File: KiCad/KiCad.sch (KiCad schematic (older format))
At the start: 18 parts

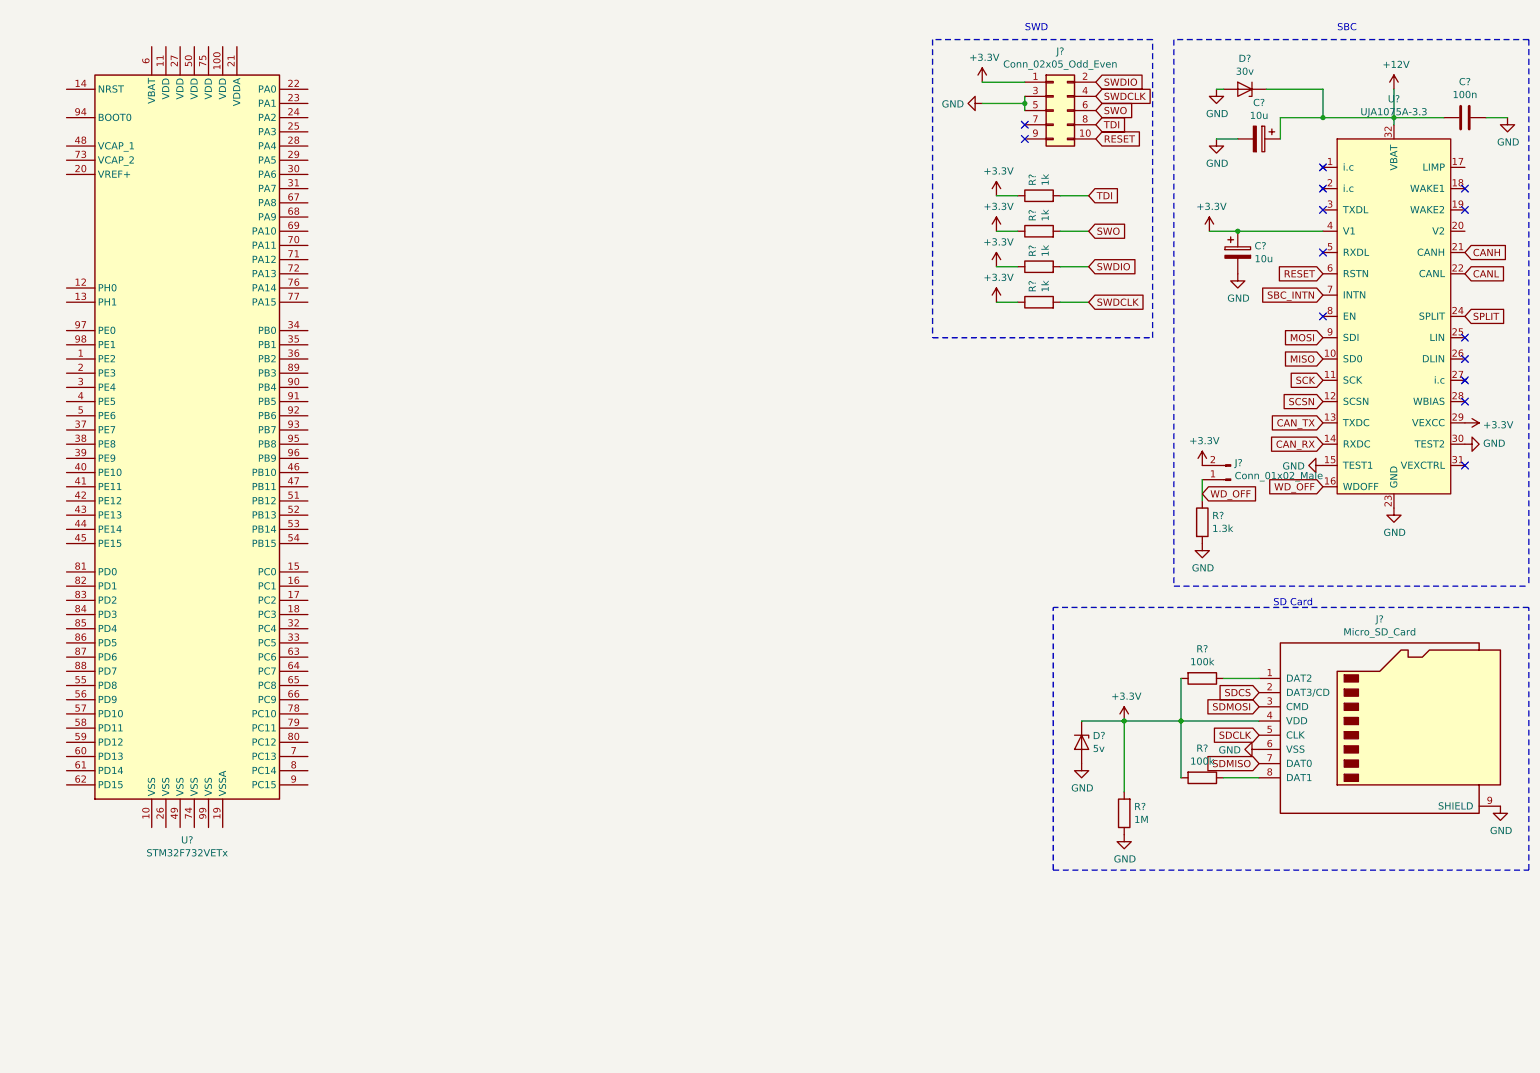
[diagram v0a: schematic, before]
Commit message: SPI, reset, CAN and status
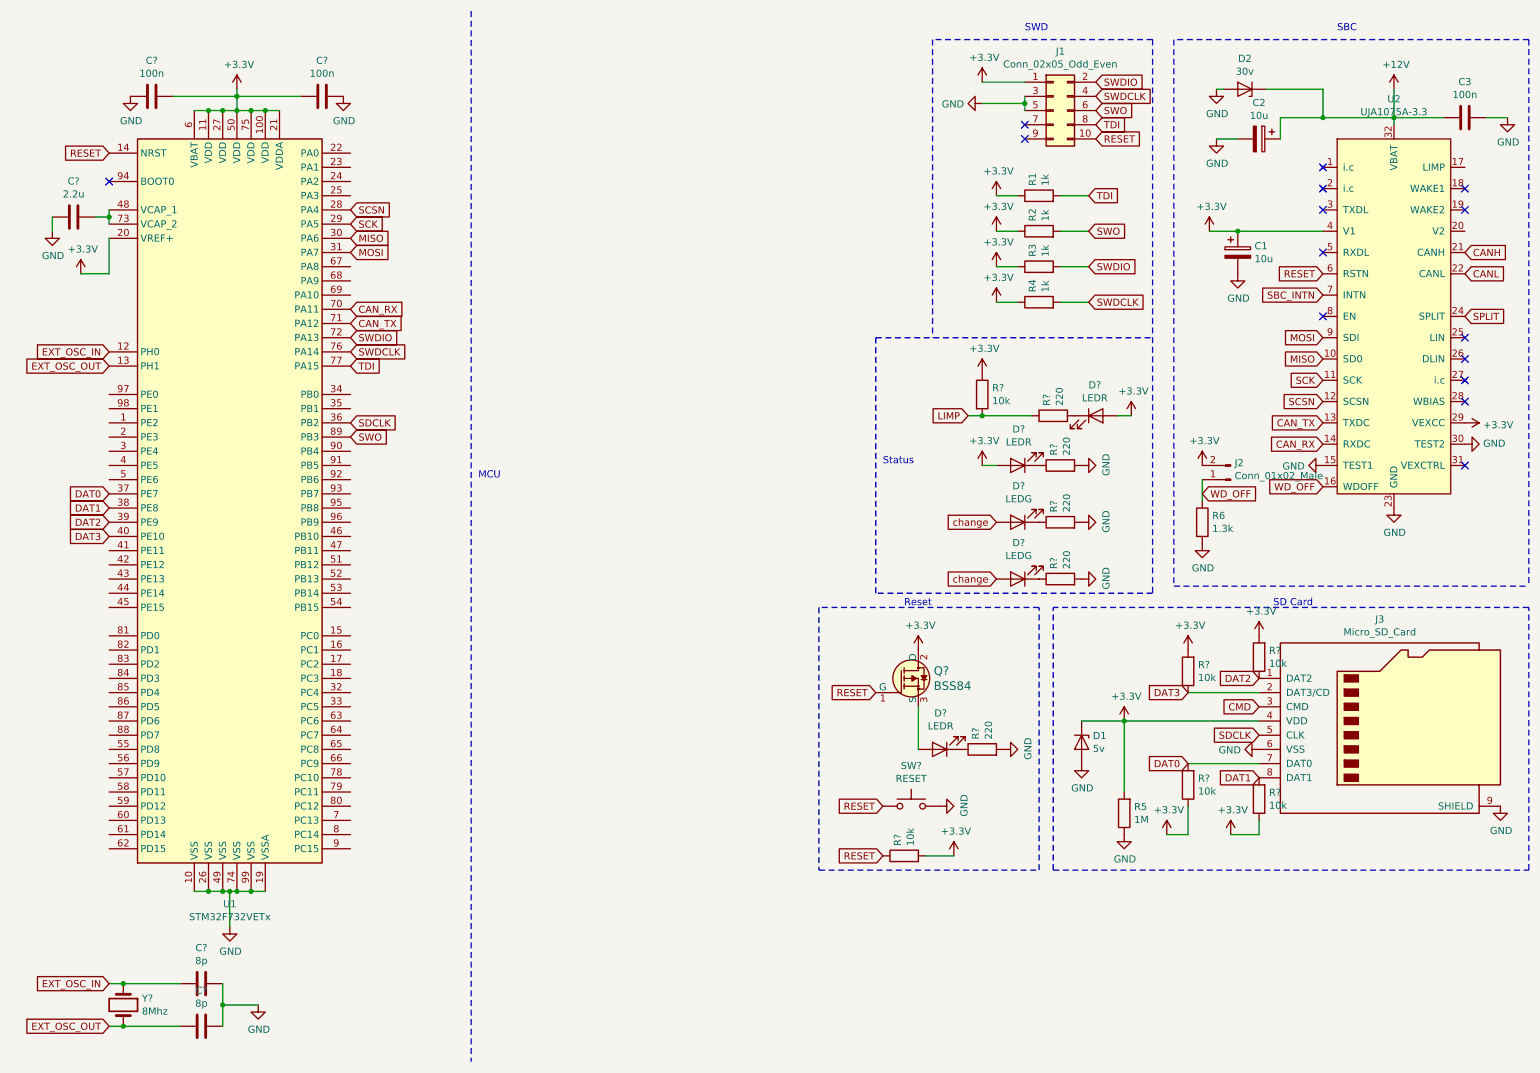
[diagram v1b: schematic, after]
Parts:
- removed R? (x2): 100k, symbol Device:R
- added C? (x2): 100n, Capacitor_SMD:C_0603_1608Metric_Pad1.05x0.95mm_HandSolder, symbol Device:C
- added C?: 2.2u, Capacitor_SMD:C_0603_1608Metric_Pad1.05x0.95mm_HandSolder, symbol Device:C
- added C? (x2): 8p, Capacitor_SMD:C_0603_1608Metric_Pad1.05x0.95mm_HandSolder, symbol Device:C
- added D? (x3): LEDR, symbol Device:LED
- added D? (x2): LEDG, symbol Device:LED
- added Q?: BSS84, digikey-footprints:SOT-23-3, symbol dk_Transistors-FETs-MOSFETs-Single:BSS84
- added R? (x5): 220, Resistor_SMD:R_0603_1608Metric_Pad1.05x0.95mm_HandSolder, symbol Device:R
- added R? (x6): 10k, Resistor_SMD:R_0603_1608Metric_Pad1.05x0.95mm_HandSolder, symbol Device:R
- added SW?: RESET, symbol Switch:SW_Push
- added Y?: 8Mhz, symbol Device:Crystal
- C1, C2, C3: renamed from C?; footprint (none) -> Capacitor_SMD:C_0603_1608Metric_Pad1.05x0.95mm_HandSolder
- R1, R2, R3, R4, R5, R6: renamed from R?; footprint (none) -> Resistor_SMD:R_0603_1608Metric_Pad1.05x0.95mm_HandSolder
- gave numbers to parts that had none: 7
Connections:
- net SDCS is gone; now on net DAT3: J3.2 (DAT3/CD)
- net SDMISO is gone; now on net DAT0: J3.7 (DAT0)
- net +3V3: now also U1.100 (VDD), U1.11 (VDD), U1.20 (VREF+), U1.21 (VDDA), U1.27 (VDD), U1.50 (VDD), U1.6 (VBAT), U1.75 (VDD), C?.1, C?.2, D?.2 (A), D?.2 (A), Q?.2 (D), R?.1, R?.1, R?.1, R?.2, R?.2, R?.2
- net CAN_RX: now also U1.70 (PA11)
- net CAN_TX: now also U1.71 (PA12)
- net GND: now also U1.10 (VSS), U1.19 (VSSA), U1.26 (VSS), U1.49 (VSS), U1.74 (VSS), U1.99 (VSS), C?.1, C?.1, C?.1, C?.2, C?.2, R?.2, R?.2, R?.2, R?.2, SW?.2
- net MISO: now also U1.30 (PA6)
- net MOSI: now also U1.31 (PA7)
- net RESET: now also U1.14 (NRST), Q?.1 (G), R?.1, SW?.1
- net SCK: now also U1.29 (PA5)
- net SCSN: now also U1.28 (PA4)
- net SDCLK: now also U1.36 (PB2)
- net SWDCLK: now also U1.76 (PA14)
- net SWDIO: now also U1.72 (PA13)
- net SWO: now also U1.89 (PB3)
- net TDI: now also U1.77 (PA15)
- net EXT_OSC_IN: now reaches U1.12 (PH0)
- net EXT_OSC_IN: now also C?.2, Y?.1
- net EXT_OSC_OUT: now reaches U1.13 (PH1)
- net EXT_OSC_OUT: now also C?.2, Y?.2
- net DAT0: now reaches U1.37 (PE7)
- net DAT0: now also R?.2
- net DAT1: now reaches U1.38 (PE8)
- net DAT1: now also J3.8 (DAT1), R?.2
- net DAT2: now reaches U1.39 (PE9)
- net DAT2: now also J3.1 (DAT2), R?.1
- net DAT3: now reaches U1.40 (PE10)
- net DAT3: now also R?.1
- net at U1.48 (VCAP_1): now also U1.73 (VCAP_2), C?.1
- net SDMOSI renamed CMD
- new net: D?.2 (A), Q?.3 (S)
- new net: D?.1 (K), R?.1 (x4)
- new net: D?.1 (K), R?.2
- new net LIMP: R?.1, R?.2
- new net change: D?.2 (A), D?.2 (A)
- no-connect marks 14 -> 15
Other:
- note added: "MCU"
- note added: "Reset"
- note added: "Status"
- moved on the sheet: U1

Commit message: Two SBCs and Autogenerated STM32cube code
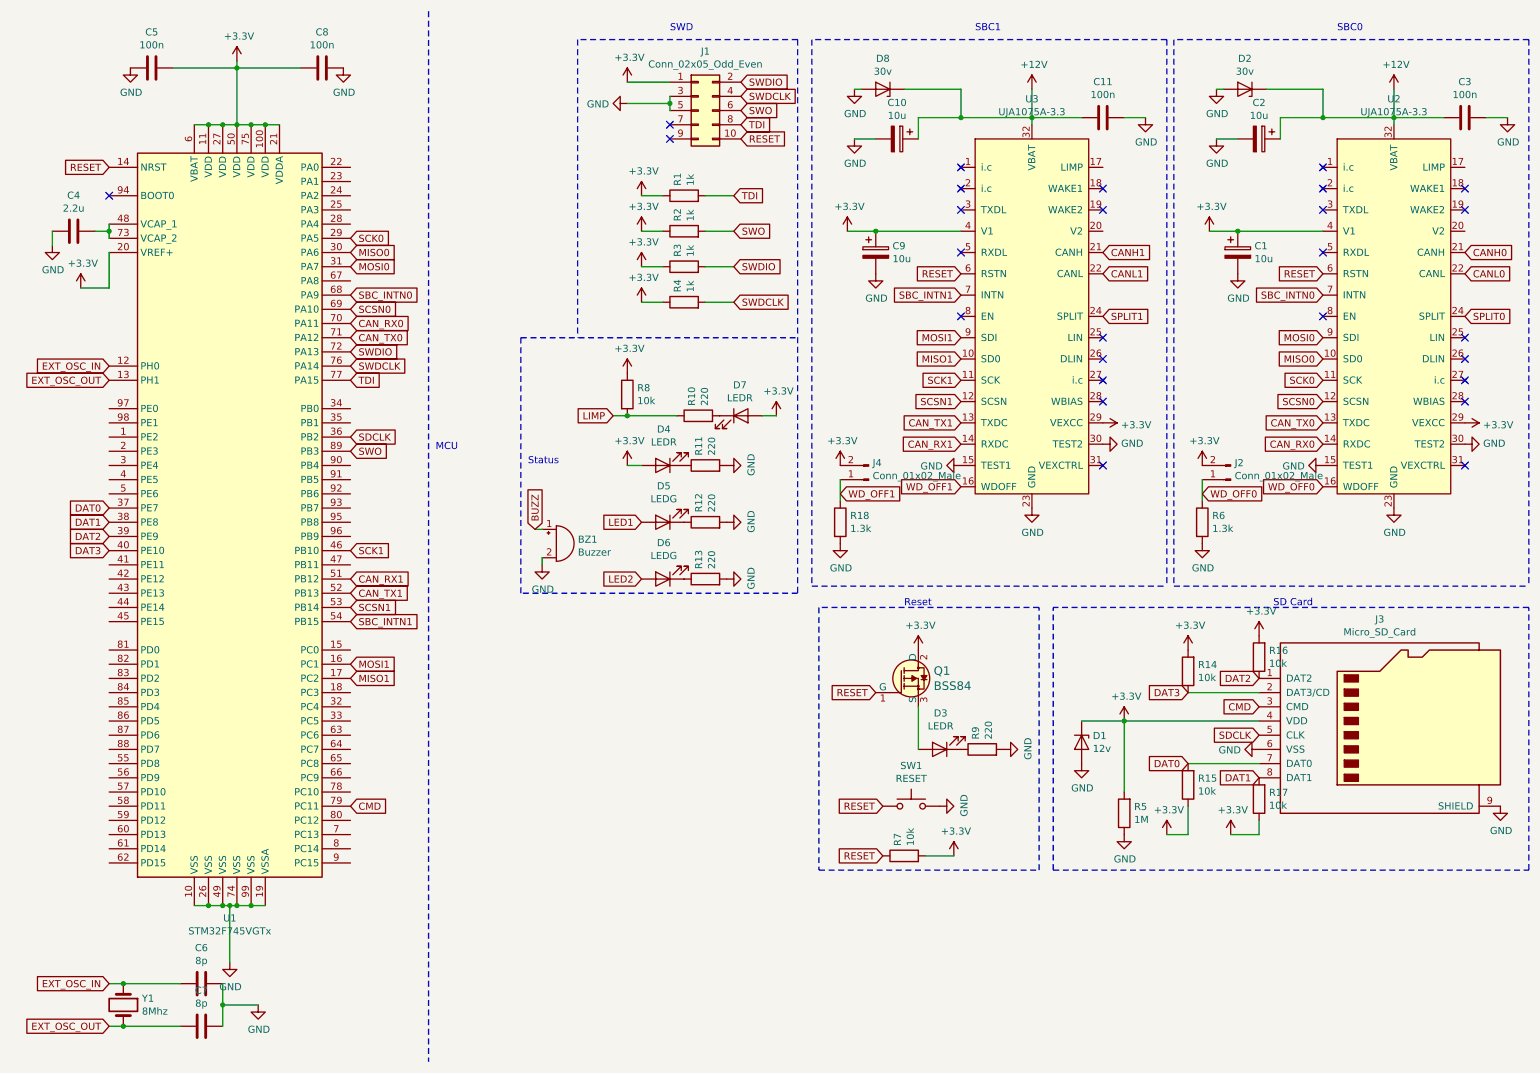
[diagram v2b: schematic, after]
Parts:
- removed U1: STM32F732VETx, Package_QFP:LQFP-100_14x14mm_P0.5mm, symbol MCU_ST_STM32F7:STM32F732VETx
- added BZ1: Buzzer, Buzzer_Beeper:Buzzer_12x9.5RM7.6, symbol Device:Buzzer
- added C10, C9: 10u, Capacitor_SMD:C_0603_1608Metric_Pad1.05x0.95mm_HandSolder, symbol Device:CP
- added C11: 100n, Capacitor_SMD:C_0603_1608Metric_Pad1.05x0.95mm_HandSolder, symbol Device:C
- added D8: 30v, Diode_SMD:D_SOD-123, symbol Device:D_Zener
- added J4: Conn_01x02_Male, Connector_PinHeader_1.27mm:PinHeader_1x02_P1.27mm_Vertical, symbol Connector:Conn_01x02_Male
- added R18: 1.3k, Resistor_SMD:R_0603_1608Metric_Pad1.05x0.95mm_HandSolder, symbol Device:R
- added U1: STM32F745VGTx, Package_QFP:LQFP-100_14x14mm_P0.5mm, symbol MCU_ST_STM32F7:STM32F745VGTx
- added U3: UJA1075A-3.3, Package_SO:HTSSOP-38-1EP_6.1x12.5mm_P0.65mm_EP5.2x12.5mm_Mask3.39x6.35mm_ThermalVias, symbol Lukas_Library:UJA1075A-3.3
- D1: value 5v -> 12v; footprint (none) -> Package_TO_SOT_SMD:SOT-23_Handsoldering
- D2: footprint (none) -> Diode_SMD:D_SOD-123
- D3, D4, D5, D6, D7: renamed from D?; footprint (none) -> Diode_SMD:D_0603_1608Metric_Pad1.05x0.95mm_HandSolder
- J1: footprint (none) -> Connector_PinHeader_1.27mm:PinHeader_2x05_P1.27mm_Vertical
- J2: footprint (none) -> Connector_PinHeader_1.27mm:PinHeader_1x02_P1.27mm_Vertical
- J3: footprint (none) -> Connector_Card:microSD_HC_Wuerth_693072010801
- SW1: renamed from SW?; footprint (none) -> Crystal:Crystal_SMD_0603-2Pin_6.0x3.5mm_HandSoldering
- Y1: renamed from Y?; footprint (none) -> Oscillator:Oscillator_SMD_Abracon_ASE-4Pin_3.2x2.5mm_HandSoldering
- gave numbers to parts that had none: 17
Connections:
- net +12V: now also C10.1, C11.2, D8.1 (K), U3.32 (VBAT)
- net +3V3: now also C9.1, J4.2 (Pin_2), U1.100 (VDD), U1.11 (VDD), U1.20 (VREF+), U1.21 (VDDA), U1.27 (VDD), U1.50 (VDD), U1.6 (VBAT), U1.75 (VDD), U3.29 (VEXCC), U3.4 (V1)
- net CMD: now also U1.79 (PC11)
- net DAT0: now also U1.37 (PE7)
- net DAT1: now also U1.38 (PE8)
- net DAT2: now also U1.39 (PE9)
- net DAT3: now also U1.40 (PE10)
- net EXT_OSC_IN: now also U1.12 (PH0)
- net EXT_OSC_OUT: now also U1.13 (PH1)
- net GND: now also BZ1.2 (+), C10.2, C11.1, C9.2, D8.2 (A), R18.2, U1.10 (VSS), U1.19 (VSSA), U1.26 (VSS), U1.49 (VSS), U1.74 (VSS), U1.99 (VSS), U3.15 (TEST1), U3.23 (GND), U3.30 (TEST2)
- net RESET: now also U1.14 (NRST), U3.6 (RSTN)
- net SDCLK: now also U1.36 (PB2)
- net SWDCLK: now also U1.76 (PA14)
- net SWDIO: now also U1.72 (PA13)
- net SWO: now also U1.89 (PB3)
- net TDI: now also U1.77 (PA15)
- net at C4.1: now also U1.48 (VCAP_1), U1.73 (VCAP_2)
- net CANH renamed CANH0
- net CANL renamed CANL0
- net CAN_RX renamed CAN_RX0
- net CAN_RX0: now also U1.70 (PA11)
- net CAN_TX renamed CAN_TX0
- net CAN_TX0: now also U1.71 (PA12)
- net MISO renamed MISO0
- net MISO0: now also U1.30 (PA6)
- net MOSI renamed MOSI0
- net MOSI0: now also U1.31 (PA7)
- net SBC_INTN renamed SBC_INTN0
- net SBC_INTN0: now also U1.68 (PA9)
- net SCK renamed SCK0
- net SCK0: now also U1.29 (PA5)
- net SCSN renamed SCSN0
- net SCSN0: now also U1.69 (PA10)
- net SPLIT renamed SPLIT0
- net WD_OFF renamed WD_OFF0
- net change renamed LED1
- net LED1: no longer D6.2 (A)
- new net BUZZ: BZ1.1 (-)
- new net CANH1: U3.21 (CANH)
- new net CANL1: U3.22 (CANL)
- new net CAN_RX1: U1.51 (PB12), U3.14 (RXDC)
- new net CAN_TX1: U1.52 (PB13), U3.13 (TXDC)
- new net LED2: D6.2 (A)
- new net MISO1: U1.17 (PC2), U3.10 (SD0)
- new net MOSI1: U1.16 (PC1), U3.9 (SDI)
- new net SBC_INTN1: U1.54 (PB15), U3.7 (INTN)
- new net SCK1: U1.46 (PB10), U3.11 (SCK)
- new net SCSN1: U1.53 (PB14), U3.12 (SCSN)
- new net SPLIT1: U3.24 (SPLIT)
- new net WD_OFF1: J4.1 (Pin_1), R18.1, U3.16 (WDOFF)
- no-connect marks 15 -> 27
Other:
- note added: "SBC0"
- note added: "SBC1"
- note removed: "SBC"
- moved on the sheet: C4, C5, C8, D4, D5, D6, D7, J1, R1, R10, R11, R12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
